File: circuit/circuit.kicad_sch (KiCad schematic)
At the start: 1 part, among them U3 RP2040

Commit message: finish circuit
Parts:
- removed U3: RP2040, RP2040_minimal:RP2040-QFN-56, symbol MCU_RaspberryPi_RP2040:RP2040
- added C1, C2: 10u, symbol Device:C
- added C10, C11, C12, C14, C4, C5, C6, C7, C8, C9: 100n, symbol Device:C
- added C13, C3: 1u, symbol Device:C
- added C15, C16: 27p, symbol Device:C
- added D1: (no value), symbol Device:LED
- added J1: USB_A, symbol Connector:USB_A
- added J2: Conn_02x03_Counter_Clockwise, symbol Connector_Generic:Conn_02x03_Counter_Clockwise
- added R1, R2: 27, symbol Device:R
- added R3: 10K, symbol Device:R
- added R4, R7, R8: 1k, symbol Device:R
- added R5, R6: 220, symbol Device:R
- added SW1: (no value), symbol Switch:SW_Push
- added U1: RP2040, Package_DFN_QFN:QFN-56-1EP_7x7mm_P0.4mm_EP3.2x3.2mm, symbol MCU_RaspberryPi:RP2040
- added U2: AMS1117-3.3, Package_TO_SOT_SMD:SOT-223-3_TabPin2, symbol Regulator_Linear:AMS1117-3.3
- added U3, U4: W25Q32JVSS, Package_SO:SOIC-8_5.3x5.3mm_P1.27mm, symbol Memory_Flash:W25Q32JVSS
- added Y1: 12MHz, symbol Device:Crystal
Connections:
- new net: D1.2 (A), R5.2
- new net: J2.3 (Pin_3), R8.1
- new net: C16.2, R4.1, Y1.2
- new net: J2.6 (Pin_6), R6.1
- new net: J1.2 (D-), R2.1
- new net: J1.3 (D+), R1.1
- new net: J2.2 (Pin_2), R7.1
- new net: C2.1, U2.2 (VO)
- new net +1V1: C3.1, C4.1, C5.1, U1.23 (DVDD), U1.45 (VREG_VOUT), U1.50 (DVDD)
- new net +3V3: C10.1, C11.1, C12.1, C13.1, C14.1, C6.1, C7.1, C8.1, C9.1, R3.2, SW1.1, U1.1 (IOVDD), U1.10 (IOVDD), U1.22 (IOVDD), U1.33 (IOVDD), U1.42 (IOVDD), U1.43 (ADC_AVDD), U1.44 (VREG_VIN), U1.48 (USB_VDD), U1.49 (IOVDD), U3.8 (VCC), U4.8 (VCC)
- new net DBG_BOOT: R3.1, R7.2, U1.56 (~{QSPI_SS}), U3.1 (~{CS})
- new net DBG_GND: J2.1 (Pin_1)
- new net DBG_LED: R6.2, U1.37 (GPIO25)
- new net DBG_RUN: R8.2, U1.26 (RUN)
- new net DBG_RX: J2.5 (Pin_5), U1.28 (GPIO17)
- new net DBG_TX: J2.4 (Pin_4), U1.27 (GPIO16)
- new net DMEM_CLK: U1.29 (GPIO18), U4.6 (CLK)
- new net DMEM_CS: U4.1 (~{CS})
- new net DMEM_DI: U1.30 (GPIO19), U4.5 (DI/IO_{0})
- new net DMEM_DO: U1.31 (GPIO20), U4.2 (DO/IO_{1})
- new net GND: C1.2, C10.2, C11.2, C12.2, C13.2, C14.2, C15.1, C16.1, C2.2, C3.2, C4.2, C5.2, C6.2, C7.2, C8.2, C9.2, D1.1 (K), J1.4 (GND), J1.SH (Shield), U1.57 (GND), U2.1 (GND), U3.4 (GND), U4.4 (GND)
- new net IO_BTN: SW1.2, U1.7 (GPIO5)
- new net IO_LED: R5.1, U1.8 (GPIO6)
- new net PMEM_CLK: U1.52 (QSPI_SCLK), U3.6 (CLK)
- new net PMEM_IO0: U1.53 (QSPI_SD0), U3.5 (DI/IO_{0})
- new net PMEM_IO1: U1.55 (QSPI_SD1), U3.2 (DO/IO_{1})
- new net PMEM_IO2: U1.54 (QSPI_SD2), U3.3 (~{WP}/IO_{2})
- new net PMEM_IO3: U1.51 (QSPI_SD3), U3.7 (~{HOLD}/~{RESET}/IO_{3})
- new net USB_D+: R1.2, U1.46 (USB_DM)
- new net USB_D-: R2.2, U1.47 (USB_DP)
- new net VBUS: C1.1, J1.1 (VBUS), U2.3 (VI)
- new net XIN: C15.2, U1.20 (XIN), Y1.1
- new net XOUT: R4.2, U1.21 (XOUT)
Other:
- note added: "All components here are for debug purposes only and should NOT be installed in consumer devices."
- note added: "Put C13 close to pin 44"
- note added: "Put C3 close to pin 45"
- note added: "Put R1 and R2 close to MCU"
- company: Chubiy Savva -> Savva Chubiy

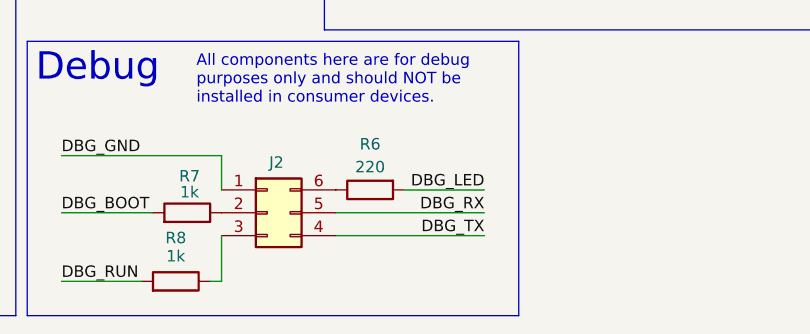
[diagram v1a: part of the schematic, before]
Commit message: connect DBG_GND and GND
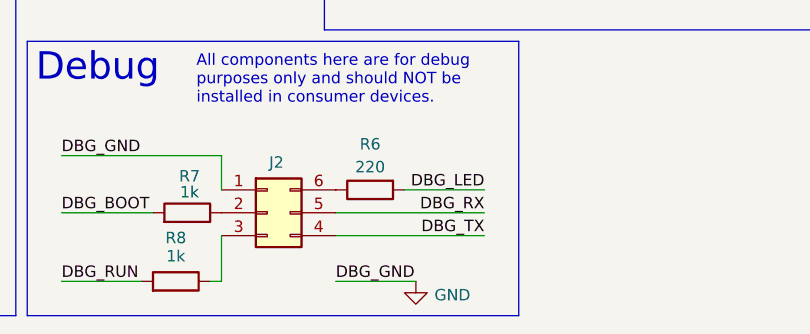
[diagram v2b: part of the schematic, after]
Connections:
- net DBG_GND is gone; now on net GND: J2.1 (Pin_1)
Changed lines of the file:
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@@
 	(wire
 		(pts
+			(xy 156.21 191.77) (xy 165.1 191.77)
+		)
+		(stroke
+			(width 0)
+			(type default)
+		)
+	)
+	(wire
+		(pts
 			(xy 160.02 104.14) (xy 170.18 104.14)
 		)
@@
 		)
 	)
+	(label "DBG_GND"
+		(at 156.21 191.77 0)
+		(effects
+			(font
+				(size 1.27 1.27)
+			)
+			(justify left bottom)
+		)
+	)
 	(label "DBG_RX"
 		(at 172.72 184.15 180)
@@
 					(unit 1)
 				)
+			)
+		)
+	)
+	(symbol
+		(lib_id "power:GND")
+		(at 165.1 191.77 0)
+		(unit 1)
+		(body_style 1)
+		(exclude_from_sim no)
+		(in_bom yes)
+		(on_board yes)
+		(in_pos_files yes)
+		(dnp no)
+		(property "Reference" "#PWR024"
+			(at 165.1 198.12 0)
+			(hide yes)
+			(show_name no)
+			(do_not_autoplace no)
+			(effects
+				(font
+					(size 1.27 1.27)
+				)
+			)
+		)
+		(property "Value" "GND"
+			(at 169.164 193.294 0)
+			(show_name no)
+			(do_not_autoplace no)
+			(effects
+				(font
+					(size 1.27 1.27)
+				)
+			)
+		)
+		(property "Footprint" ""
+			(at 165.1 191.77 0)
+			(hide yes)
+			(show_name no)
+			(do_not_autoplace no)
+			(effects
+				(font
+					(size 1.27 1.27)
+				)
+			)
+		)
+		(property "Datasheet" ""
+			(at 165.1 191.77 0)
+			(hide yes)
+			(show_name no)
+			(do_not_autoplace no)
+			(effects
+				(font
+					(size 1.27 1.27)
+				)
+			)
+		)
+		(property "Description" "Power symbol creates a global label with name \"GND\" , ground"
+			(at 165.1 191.77 0)
+			(hide yes)
+			(show_name no)
+			(do_not_autoplace no)
+			(effects
+				(font
+					(size 1.27 1.27)
+				)
+			)
+		)
+		(pin "1"
+		)
+		(instances
+			(project "circuit"
+				(path "/8ff94e83-2bff-4482-b0f5-a16df1951a9e"
+					(reference "#PWR024")
+					(unit 1)
+				)

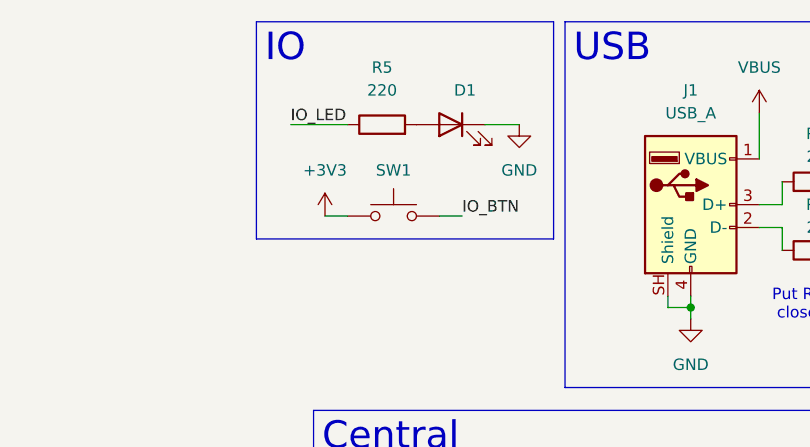
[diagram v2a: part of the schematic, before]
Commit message: fix pull-up connected button
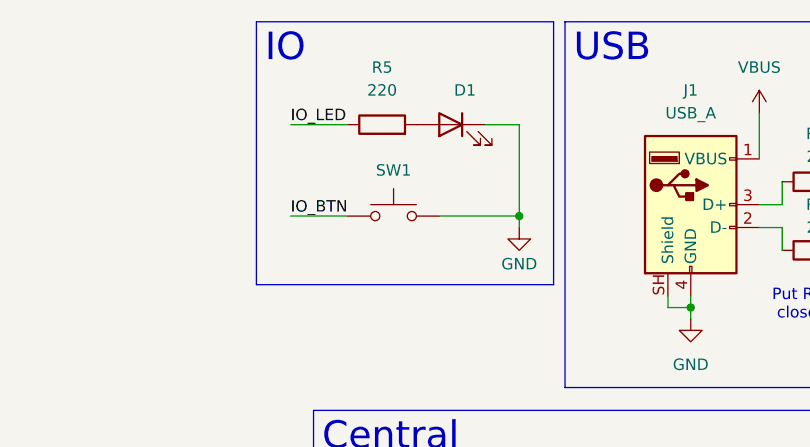
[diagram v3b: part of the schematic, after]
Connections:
- net +3V3: no longer SW1.1
- net GND: now also SW1.2
- net IO_BTN: now also SW1.1; no longer SW1.2
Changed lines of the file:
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@@
 		(exclude_from_sim no)
 		(at 148.59 13.97 0)
-		(size 33.02 24.13)
+		(size 33.02 29.21)
 		(margins 0.9525 0.9525 0.9525 0.9525)
 		(stroke
@@
 	)
 	(junction
+		(at 177.8 35.56)
+		(diameter 0)
+		(color 0 0 0 0)
+	)
+	(junction
 		(at 92.71 173.99)
 		(diameter 0)
@@
 	(wire
 		(pts
+			(xy 177.8 25.4) (xy 173.99 25.4)
+		)
+		(stroke
+			(width 0)
+			(type default)
+		)
+	)
+	(wire
+		(pts
 			(xy 185.42 139.7) (xy 163.83 139.7)
 		)
@@
 	(wire
 		(pts
+			(xy 168.91 35.56) (xy 177.8 35.56)
+		)
+		(stroke
+			(width 0)
+			(type default)
+		)
+	)
+	(wire
+		(pts
 			(xy 270.51 119.38) (xy 281.94 119.38)
 		)
@@
 	(wire
 		(pts
-			(xy 156.21 35.56) (xy 158.75 35.56)
+			(xy 152.4 35.56) (xy 158.75 35.56)
 		)
 		(stroke
@@
 	(wire
 		(pts
-			(xy 168.91 35.56) (xy 171.45 35.56)
-		)
-		(stroke
-			(width 0)
-			(type default)
-		)
-	)
-	(wire
-		(pts
 			(xy 212.09 99.06) (xy 219.71 99.06)
 		)
@@
 	(wire
 		(pts
+			(xy 177.8 35.56) (xy 177.8 25.4)
+		)
+		(stroke
+			(width 0)
+			(type default)
+		)
+	)
+	(wire
+		(pts
 			(xy 40.64 158.75) (xy 53.34 158.75)
 		)
@@
 	(wire
 		(pts
+			(xy 177.8 36.83) (xy 177.8 35.56)
+		)
+		(stroke
+			(width 0)
+			(type default)
+		)
+	)
+	(wire
+		(pts
 			(xy 17.78 151.13) (xy 29.21 151.13)
 		)
@@
 		(pts
 			(xy 170.18 90.17) (xy 171.45 90.17)
-		)
-		(stroke
-			(width 0)
-			(type default)
-		)
-	)
-	(wire
-		(pts
-			(xy 173.99 25.4) (xy 177.8 25.4)
 		)
 		(stroke
@@
 		)
 	)
-	(label "IO_BTN"
-		(at 171.45 35.56 0)
-		(effects
-			(font
-				(size 1.27 1.27)
-			)
-			(justify left bottom)
-		)
-	)
 	(label "PMEM_IO3"
 		(at 208.28 121.92 0)
@@
 	(label "XIN"
 		(at 214.63 129.54 0)
+		(effects
+			(font
+				(size 1.27 1.27)
+			)
+			(justify left bottom)
+		)
+	)
+	(label "IO_BTN"
+		(at 152.4 35.56 0)
 		(effects
 			(font
@@
 	(symbol
 		(lib_id "power:GND")
-		(at 177.8 25.4 0)
+		(at 177.8 36.83 0)
 		(unit 1)
 		(body_style 1)
@@
 		(in_pos_files yes)
 		(dnp no)
-		(fields_autoplaced yes)
 		(property "Reference" "#PWR022"
-			(at 177.8 31.75 0)
+			(at 177.8 43.18 0)
 			(hide yes)
 			(show_name no)
@@
 		)
 		(property "Value" "GND"
-			(at 177.8 30.48 0)
+			(at 177.8 40.894 0)
 			(show_name no)
 			(do_not_autoplace no)
@@
 		)
 		(property "Footprint" ""
-			(at 177.8 25.4 0)
+			(at 177.8 36.83 0)
 			(hide yes)
 			(show_name no)
@@
 		)
 		(property "Datasheet" ""
-			(at 177.8 25.4 0)
+			(at 177.8 36.83 0)
 			(hide yes)
 			(show_name no)
@@
 		)
 		(property "Description" "Power symbol creates a global label with name \"GND\" , ground"
-			(at 177.8 25.4 0)
+			(at 177.8 36.83 0)
 			(hide yes)
 			(show_name no)
@@
 					(unit 1)
 				)
-			)
-		)
-	)
-	(symbol
-		(lib_id "power:+3V3")
-		(at 156.21 35.56 0)
-		(unit 1)
-		(body_style 1)
-		(exclude_from_sim no)
-		(in_bom yes)
-		(on_board yes)
-		(in_pos_files yes)
-		(dnp no)
-		(fields_autoplaced yes)
-		(property "Reference" "#PWR021"
-			(at 156.21 39.37 0)
-			(hide yes)
-			(show_name no)
-			(do_not_autoplace no)
-			(effects
-				(font
-					(size 1.27 1.27)
-				)
-			)
-		)
-		(property "Value" "+3V3"
-			(at 156.21 30.48 0)
-			(show_name no)
-			(do_not_autoplace no)
-			(effects
-				(font
-					(size 1.27 1.27)
-				)
-			)
-		)
-		(property "Footprint" ""
-			(at 156.21 35.56 0)
-			(hide yes)
-			(show_name no)
-			(do_not_autoplace no)
-			(effects
-				(font
-					(size 1.27 1.27)
-				)
-			)
-		)
-		(property "Datasheet" ""
-			(at 156.21 35.56 0)
-			(hide yes)
-			(show_name no)
-			(do_not_autoplace no)
-			(effects
-				(font
-					(size 1.27 1.27)
-				)
-			)
-		)
-		(property "Description" "Power symbol creates a global label with name \"+3V3\""
-			(at 156.21 35.56 0)
-			(hide yes)
-			(show_name no)
-			(do_not_autoplace no)
-			(effects
-				(font
-					(size 1.27 1.27)
-				)
-			)
-		)
-		(pin "1"
-		)
-		(instances
-			(project "circuit"
-				(path "/8ff94e83-2bff-4482-b0f5-a16df1951a9e"
-					(reference "#PWR021")
-					(unit 1)
-				)

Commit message: fix power block
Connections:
- net +3V3: now also C2.1, U2.2 (VO)
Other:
- note added: "Put C13 close to MCU pin"
- note added: "Put C3 close to MCU pin"
- note removed: "Put C13 close to pin 44"
- note removed: "Put C3 close to pin 45"
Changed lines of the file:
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@@
 		)
 	)
-	(text "Put C3 close\nto pin 45"
+	(text "Put C3 close\nto MCU pin"
 		(exclude_from_sim no)
 		(at 72.898 180.848 0)
@@
 		)
 	)
-	(text "Put C13 close\nto pin 44"
+	(text "Put C13 close\nto MCU pin\n"
 		(exclude_from_sim no)
 		(at 112.014 161.544 0)
@@
 	)
 	(junction
+		(at 55.88 176.53)
+		(diameter 0)
+		(color 0 0 0 0)
+	)
+	(junction
 		(at 82.55 173.99)
 		(diameter 0)
@@
 		(pts
 			(xy 143.51 191.77) (xy 143.51 186.69)
+		)
+		(stroke
+			(width 0)
+			(type default)
+		)
+	)
+	(wire
+		(pts
+			(xy 55.88 171.45) (xy 55.88 176.53)
 		)
 		(stroke
@@
 					(unit 1)
 				)
+			)
+		)
+	)
+	(symbol
+		(lib_id "power:+3V3")
+		(at 55.88 171.45 0)
+		(unit 1)
+		(body_style 1)
+		(exclude_from_sim no)
+		(in_bom yes)
+		(on_board yes)
+		(in_pos_files yes)
+		(dnp no)
+		(fields_autoplaced yes)
+		(property "Reference" "#PWR021"
+			(at 55.88 175.26 0)
+			(hide yes)
+			(show_name no)
+			(do_not_autoplace no)
+			(effects
+				(font
+					(size 1.27 1.27)
+				)
+			)
+		)
+		(property "Value" "+3V3"
+			(at 55.88 166.37 0)
+			(show_name no)
+			(do_not_autoplace no)
+			(effects
+				(font
+					(size 1.27 1.27)
+				)
+			)
+		)
+		(property "Footprint" ""
+			(at 55.88 171.45 0)
+			(hide yes)
+			(show_name no)
+			(do_not_autoplace no)
+			(effects
+				(font
+					(size 1.27 1.27)
+				)
+			)
+		)
+		(property "Datasheet" ""
+			(at 55.88 171.45 0)
+			(hide yes)
+			(show_name no)
+			(do_not_autoplace no)
+			(effects
+				(font
+					(size 1.27 1.27)
+				)
+			)
+		)
+		(property "Description" "Power symbol creates a global label with name \"+3V3\""
+			(at 55.88 171.45 0)
+			(hide yes)
+			(show_name no)
+			(do_not_autoplace no)
+			(effects
+				(font
+					(size 1.27 1.27)
+				)
+			)
+		)
+		(pin "1"
+		)
+		(instances
+			(project "circuit"
+				(path "/8ff94e83-2bff-4482-b0f5-a16df1951a9e"
+					(reference "#PWR021")
+					(unit 1)
+				)
